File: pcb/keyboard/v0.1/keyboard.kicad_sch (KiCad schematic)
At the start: 123 parts, among them J1 USB2.0, J2 SWD, SW1 TAB, SW10 O, SW11 P, SW12 RETURN, SW13 CAPS, SW14 A, SW15 S, SW16 D, SW17 F, SW18 G, SW19 H, SW2 Q, SW20 J, SW21 K, SW22 L, SW23 SEMI, SW24 QUOTE, SW25 LSHIFT, SW26 Z, SW27 X, SW28 C, SW29 V, SW3 W, SW30 B, SW31 N, SW32 M, SW33 COMMA, SW34 DOT, SW35 QUEST, SW36 RSHIFT, SW37 FN, SW38 LCTRL, SW39 LSUPER, SW4 E, SW40 LALT, SW41 SPACE, SW42 SPACE, SW43 RALT, SW44 RSUPER, SW45 C8, SW46 RCTRL, SW47 C1, SW48 C2, SW49 C3, SW5 R, SW50 C4, SW51 C5, SW52 C6, SW53 C7, SW6 T, SW7 Y, SW8 U, SW9 I, U1 MDBT50Q-P1MV2, Y1 32.768

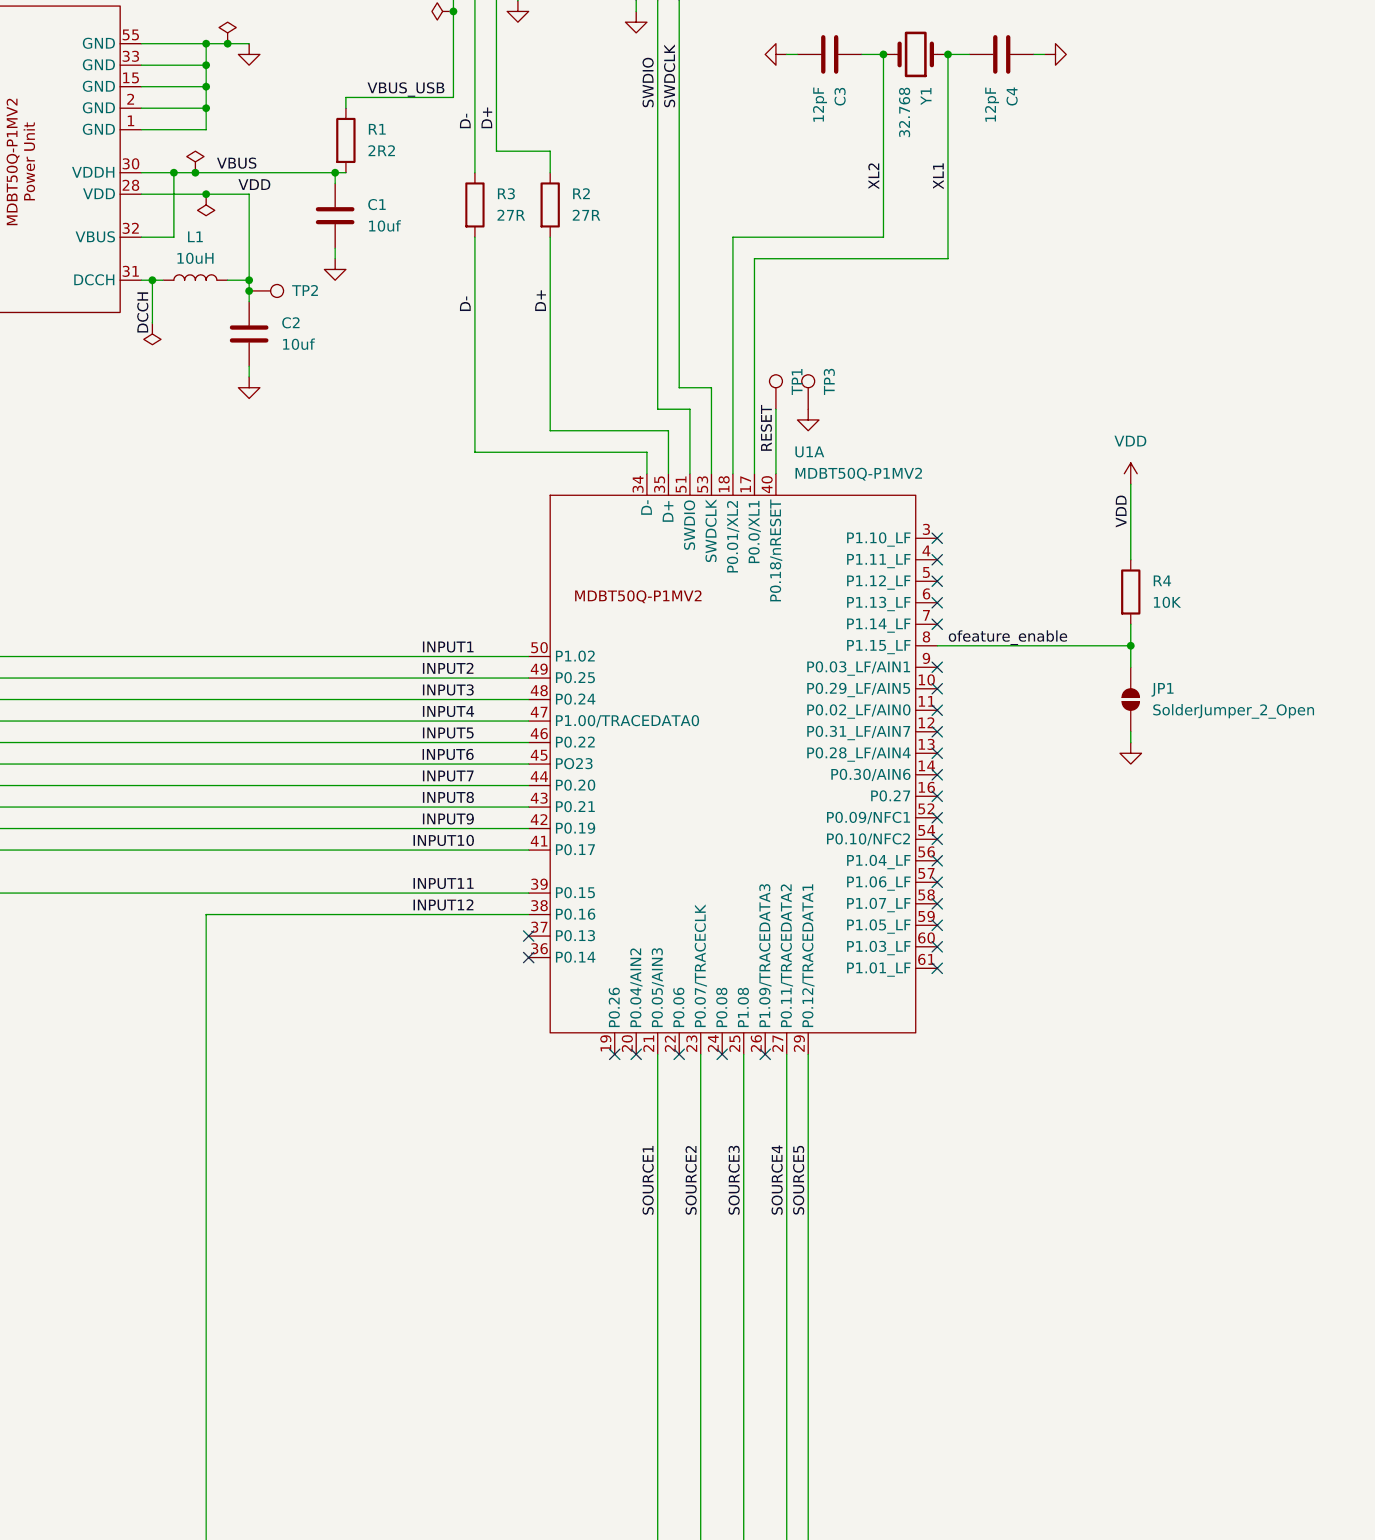
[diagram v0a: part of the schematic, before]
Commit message: Basic power circuitry done
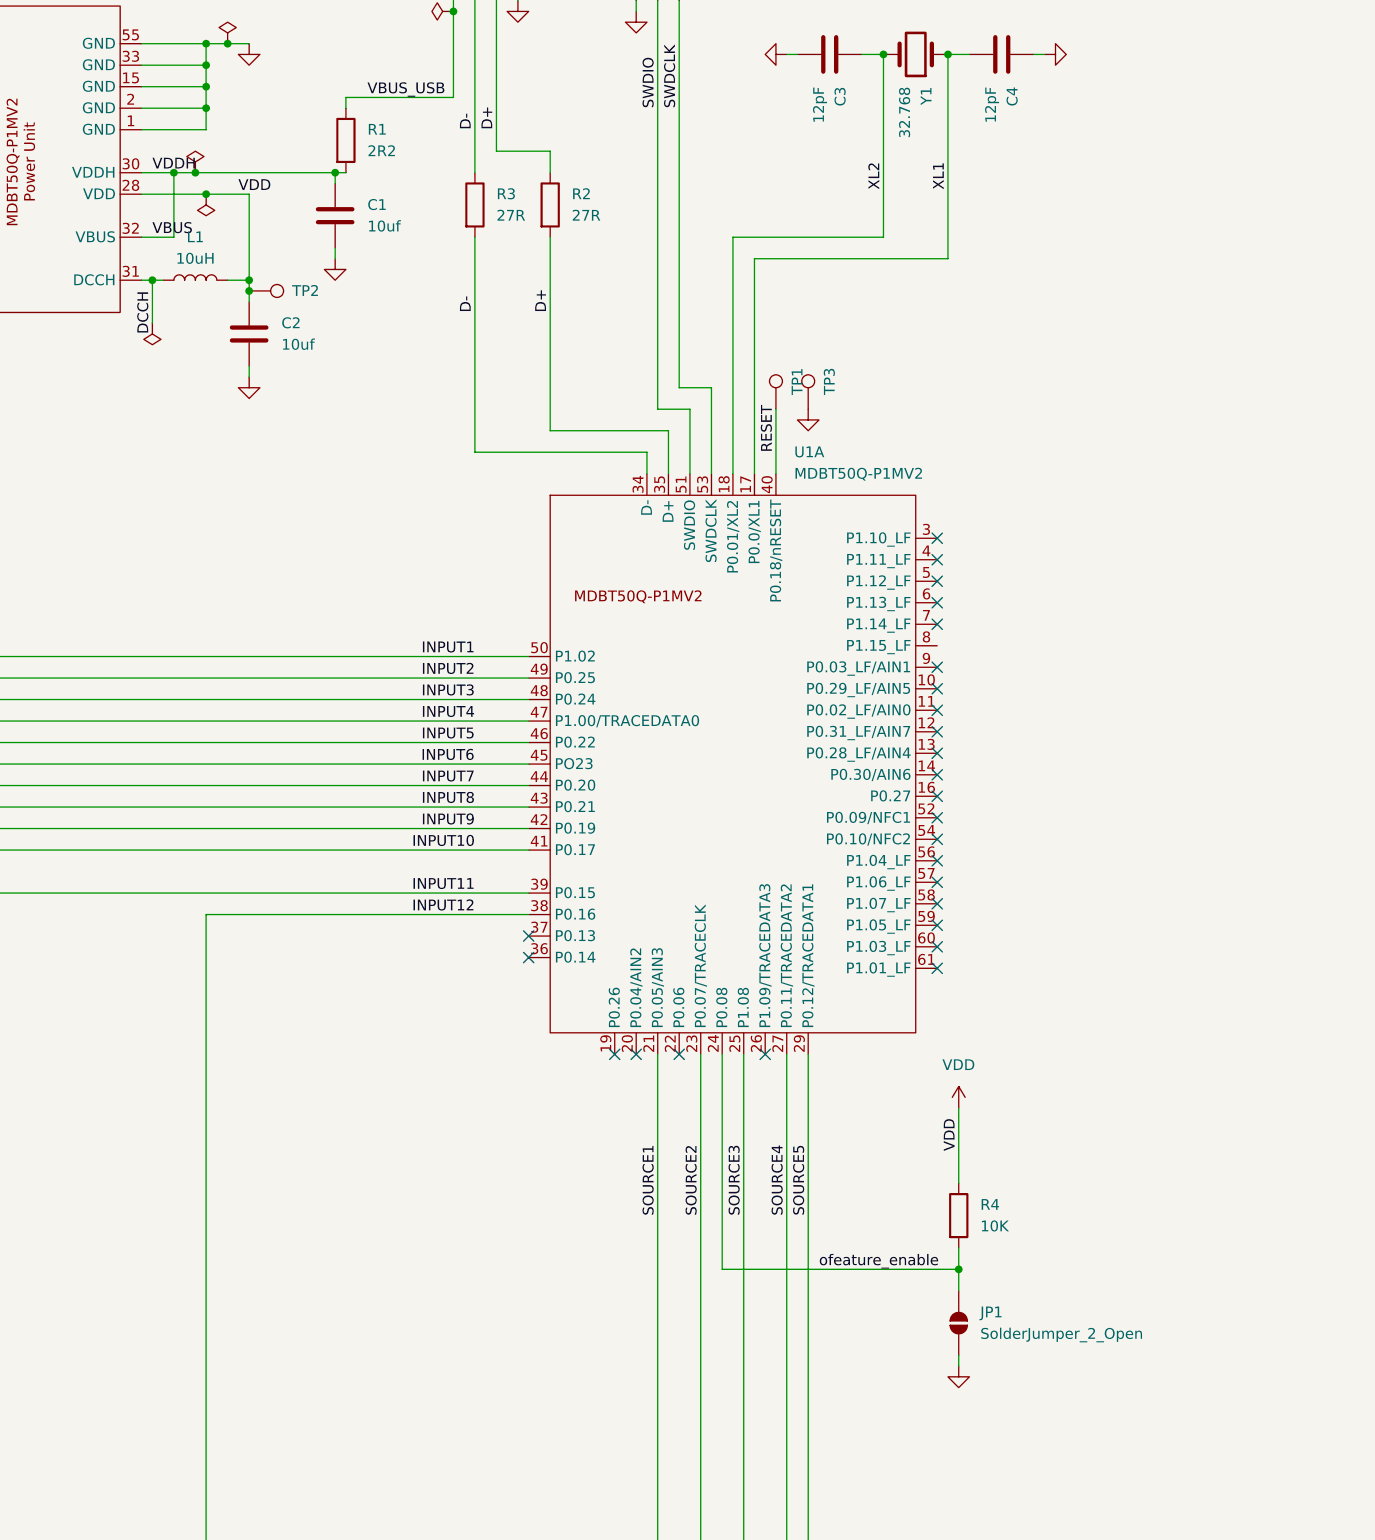
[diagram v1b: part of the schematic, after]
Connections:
- net ofeature_enable: now also U1.24 (P0.08); no longer U1.8 (P1.15_LF)
- no-connect marks 27 -> 26
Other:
- moved on the sheet: JP1, R4
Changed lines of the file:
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@@
 	)
 	(junction
+		(at 533.4 190.5)
+		(diameter 0)
+		(color 0 0 0 0)
+	)
+	(junction
 		(at 177.8 228.6)
 		(diameter 0)
@@
 	)
 	(junction
-		(at 553.72 116.84)
-		(diameter 0)
-		(color 0 0 0 0)
-	)
-	(junction
 		(at 228.6 254)
 		(diameter 0)
@@
 	)
 	(no_connect
-		(at 505.46 165.1)
-	)
-	(no_connect
 		(at 530.86 121.92)
 	)
@@
 	(wire
 		(pts
-			(xy 553.72 127) (xy 553.72 128.27)
+			(xy 533.4 200.66) (xy 533.4 201.93)
 		)
 		(stroke
@@
 	(wire
 		(pts
-			(xy 553.72 97.79) (xy 553.72 106.68)
+			(xy 533.4 171.45) (xy 533.4 180.34)
 		)
 		(stroke
@@
 	(wire
 		(pts
-			(xy 553.72 116.84) (xy 553.72 119.38)
+			(xy 533.4 187.96) (xy 533.4 190.5)
 		)
 		(stroke
@@
 	(wire
 		(pts
+			(xy 505.46 190.5) (xy 533.4 190.5)
+		)
+		(stroke
+			(width 0)
+			(type default)
+		)
+	)
+	(wire
+		(pts
 			(xy 419.1 284.48) (xy 419.1 309.88)
 		)
@@
 	(wire
 		(pts
-			(xy 436.88 63.5) (xy 444.5 63.5)
+			(xy 505.46 165.1) (xy 505.46 190.5)
 		)
 		(stroke
@@
 	(wire
 		(pts
-			(xy 241.3 284.48) (xy 241.3 309.88)
+			(xy 436.88 63.5) (xy 444.5 63.5)
 		)
 		(stroke
@@
 	(wire
 		(pts
-			(xy 532.13 71.12) (xy 509.27 71.12)
+			(xy 533.4 190.5) (xy 533.4 193.04)
 		)
 		(stroke
@@
 	(wire
 		(pts
-			(xy 485.14 58.42) (xy 485.14 60.96)
+			(xy 241.3 284.48) (xy 241.3 309.88)
 		)
 		(stroke
@@
 	(wire
 		(pts
-			(xy 485.14 91.44) (xy 499.11 91.44)
+			(xy 532.13 71.12) (xy 509.27 71.12)
 		)
 		(stroke
@@
 	(wire
 		(pts
-			(xy 215.9 233.68) (xy 215.9 259.08)
+			(xy 485.14 58.42) (xy 485.14 60.96)
 		)
 		(stroke
@@
 	(wire
 		(pts
-			(xy 530.86 116.84) (xy 553.72 116.84)
+			(xy 485.14 91.44) (xy 499.11 91.44)
 		)
 		(stroke
@@
 	(wire
 		(pts
-			(xy 355.6 279.4) (xy 381 279.4)
+			(xy 215.9 233.68) (xy 215.9 259.08)
 		)
 		(stroke
@@
 	(wire
 		(pts
-			(xy 436.88 60.96) (xy 440.69 60.96)
+			(xy 355.6 279.4) (xy 381 279.4)
 		)
 		(stroke
@@
 	(wire
 		(pts
-			(xy 444.5 233.68) (xy 444.5 259.08)
+			(xy 436.88 60.96) (xy 440.69 60.96)
 		)
 		(stroke
@@
 	(wire
 		(pts
-			(xy 553.72 114.3) (xy 553.72 116.84)
+			(xy 444.5 233.68) (xy 444.5 259.08)
 		)
 		(stroke
@@
 	)
 	(label "VDD"
-		(at 553.72 102.87 90)
+		(at 533.4 176.53 90)
 		(effects
 			(font
@@
 	)
 	(label "VBUS"
-		(at 445.77 60.96 0)
+		(at 438.15 68.58 0)
 		(effects
 			(font
@@
 	)
 	(label "ofeature_enable"
-		(at 532.13 116.84 0)
+		(at 516.89 190.5 0)
 		(effects
 			(font
@@
 		)
 	)
+	(label "VDDH"
+		(at 438.15 60.96 0)
+		(effects
+			(font
+				(size 1.27 1.27)
+			)
+			(justify left bottom)
+		)
+	)
 	(symbol
 		(lib_id "Device:D")
@@
 	(symbol
 		(lib_id "power:GND")
-		(at 553.72 128.27 0)
+		(at 533.4 201.93 0)
 		(unit 1)
 		(exclude_from_sim no)
@@
 		(fields_autoplaced yes)
 		(property "Reference" "#PWR08"
-			(at 553.72 134.62 0)
+			(at 533.4 208.28 0)
 			(effects
 				(font
@@
 		)
 		(property "Value" "GND"
-			(at 553.72 133.35 0)
+			(at 533.4 207.01 0)
 			(effects
 				(font
@@
 		)
 		(property "Footprint" ""
-			(at 553.72 128.27 0)
+			(at 533.4 201.93 0)
 			(effects
 				(font
@@
 		)
 		(property "Datasheet" ""
-			(at 553.72 128.27 0)
+			(at 533.4 201.93 0)
 			(effects
 				(font
@@
 		)
 		(property "Description" "Power symbol creates a global label with name \"GND\" , ground"
-			(at 553.72 128.27 0)
+			(at 533.4 201.93 0)
 			(effects
 				(font
@@
 	(symbol
 		(lib_id "Jumper:SolderJumper_2_Open")
-		(at 553.72 123.19 90)
+		(at 533.4 196.85 90)
 		(unit 1)
 		(exclude_from_sim no)
@@
 		(fields_autoplaced yes)
 		(property "Reference" "JP1"
-			(at 556.26 121.9199 90)
+			(at 535.94 195.5799 90)
 			(effects
 				(font
@@
 		)
 		(property "Value" "SolderJumper_2_Open"
-			(at 556.26 124.4599 90)
+			(at 535.94 198.1199 90)
 			(effects
 				(font
@@
 		)
 		(property "Footprint" "Jumper:SolderJumper-2_P1.3mm_Open_TrianglePad1.0x1.5mm"
-			(at 553.72 123.19 0)
+			(at 533.4 196.85 0)
 			(effects
 				(font
@@
 		)
 		(property "Datasheet" "~"
-			(at 553.72 123.19 0)
+			(at 533.4 196.85 0)
 			(effects
 				(font
@@
 		)
 		(property "Description" "Solder Jumper, 2-pole, open"
-			(at 553.72 123.19 0)
+			(at 533.4 196.85 0)
 			(effects
 				(font
@@
 	(symbol
 		(lib_id "power:VDD")
-		(at 553.72 97.79 0)
+		(at 533.4 171.45 0)
 		(unit 1)
 		(exclude_from_sim no)
@@
 		(fields_autoplaced yes)
 		(property "Reference" "#PWR09"
-			(at 553.72 101.6 0)
+			(at 533.4 175.26 0)
 			(effects
 				(font
@@
 		)
 		(property "Value" "VDD"
-			(at 553.72 92.71 0)
+			(at 533.4 166.37 0)
 			(effects
 				(font
@@
 		)
 		(property "Footprint" ""
-			(at 553.72 97.79 0)
+			(at 533.4 171.45 0)
 			(effects
 				(font
@@
 		)
 		(property "Datasheet" ""
-			(at 553.72 97.79 0)
+			(at 533.4 171.45 0)
 			(effects
 				(font
@@
 		)
 		(property "Description" "Power symbol creates a global label with name \"VDD\""
-			(at 553.72 97.79 0)
+			(at 533.4 171.45 0)
 			(effects
 				(font
@@
 	(symbol
 		(lib_id "Device:R")
-		(at 553.72 110.49 0)
+		(at 533.4 184.15 0)
 		(unit 1)
 		(exclude_from_sim no)
@@
 		(fields_autoplaced yes)
 		(property "Reference" "R4"
-			(at 556.26 109.2199 0)
+			(at 535.94 182.8799 0)
 			(effects
 				(font
@@
 		)
 		(property "Value" "10K"
-			(at 556.26 111.7599 0)
+			(at 535.94 185.4199 0)
 			(effects
 				(font
@@
 		)
 		(property "Footprint" "Resistor_SMD:R_0603_1608Metric"
-			(at 551.942 110.49 90)
+			(at 531.622 184.15 90)
 			(effects
 				(font
@@
 		)
 		(property "Datasheet" "~"
-			(at 553.72 110.49 0)
+			(at 533.4 184.15 0)
 			(effects
 				(font
@@
 		)
 		(property "Description" "Resistor"
-			(at 553.72 110.49 0)
+			(at 533.4 184.15 0)
 			(effects
 				(font
@@
 		)
 		(property "Manufacturer" "YAGEO"
-			(at 553.72 110.49 0)
+			(at 533.4 184.15 0)
 			(effects
 				(font
@@
 		)
 		(property "Mfr. Part no." "RC0603FR-0710KL"
-			(at 553.72 110.49 0)
+			(at 533.4 184.15 0)
 			(effects
 				(font
@@
 		)
 		(property "LCSC Part no." "C98220"
-			(at 553.72 110.49 0)
+			(at 533.4 184.15 0)
 			(effects
 				(font
@@
 		)
 		(property "Distributor Link" "https://www.lcsc.com/product-detail/C98220.html"
-			(at 553.72 110.49 0)
+			(at 533.4 184.15 0)
 			(effects
 				(font
